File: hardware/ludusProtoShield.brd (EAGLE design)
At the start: 59.7 x 53.3 mm, 54 parts, among them U1 ARDUINO, U3 TB6612FNG

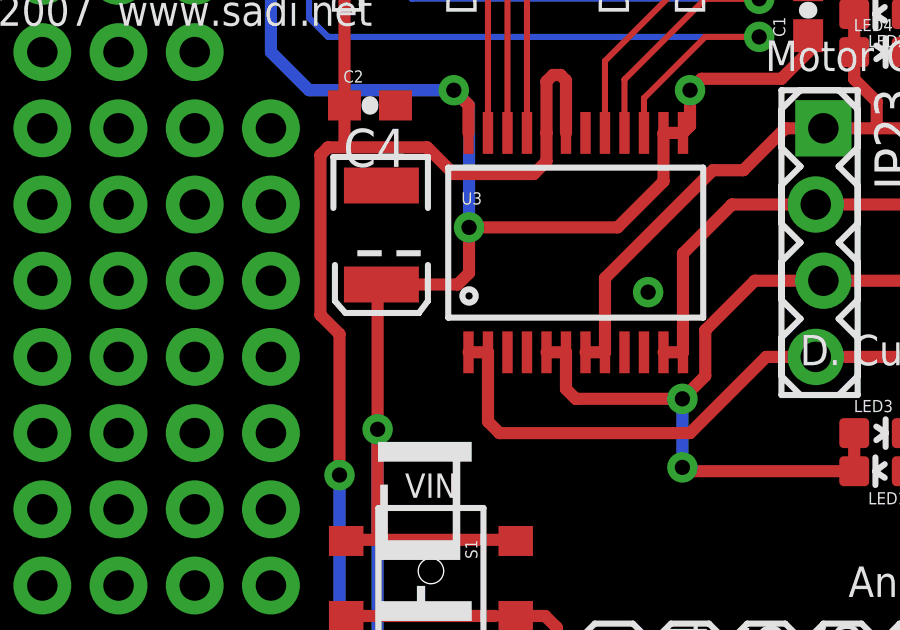
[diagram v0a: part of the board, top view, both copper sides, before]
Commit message: Fixed ERC & Board Consistency errors
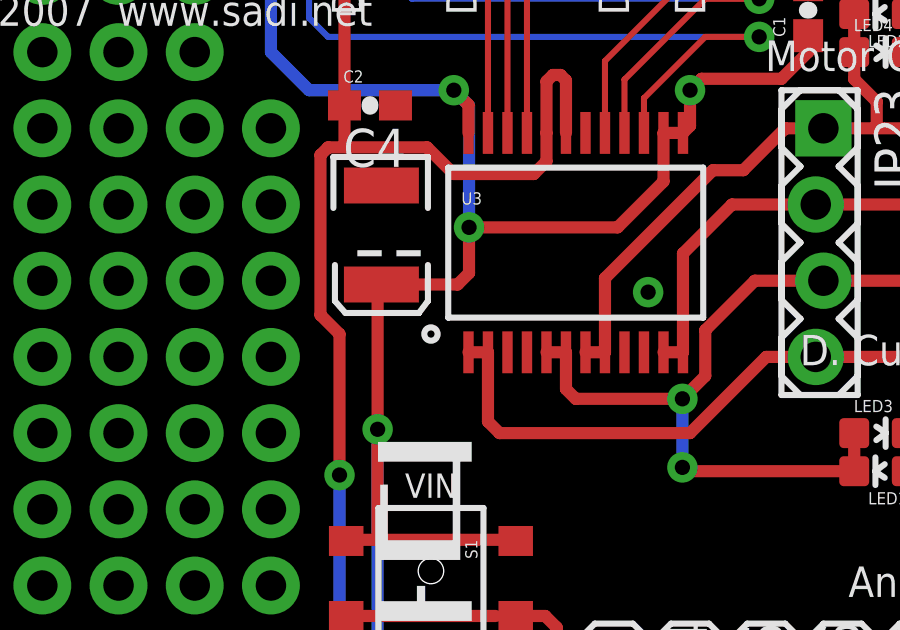
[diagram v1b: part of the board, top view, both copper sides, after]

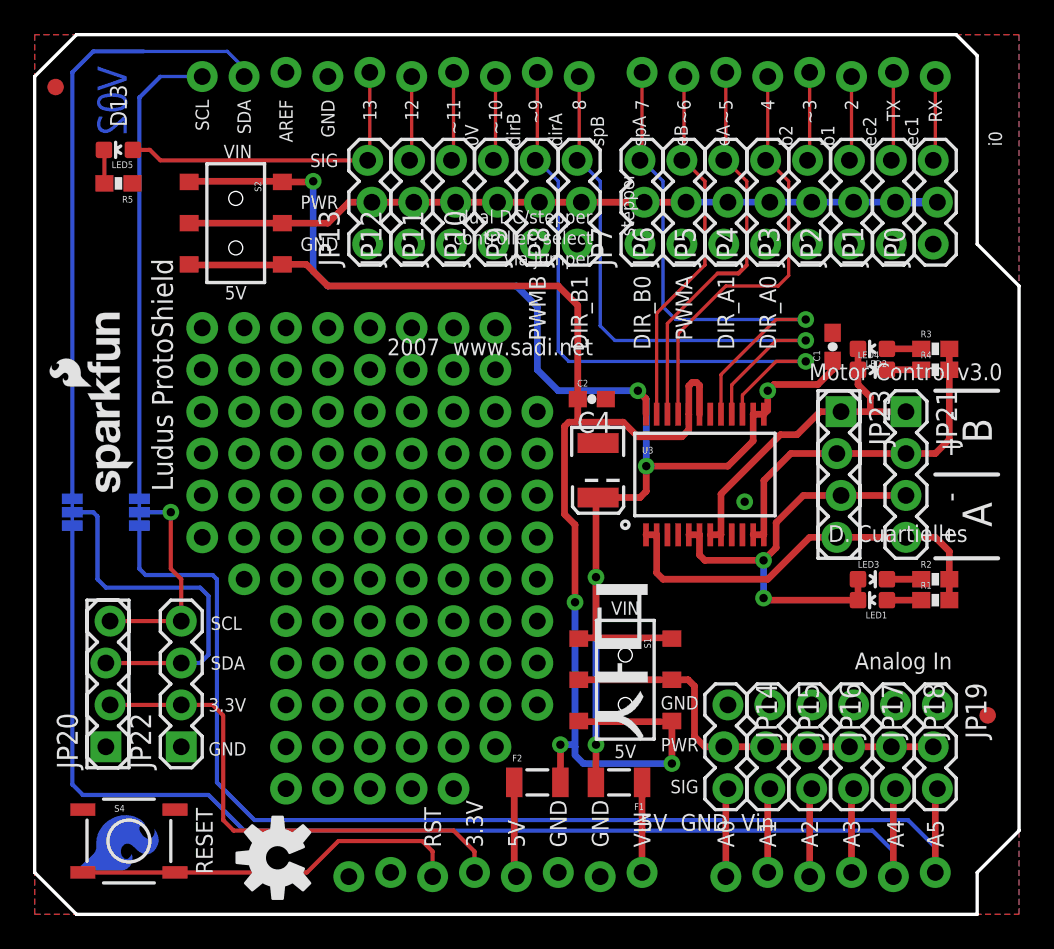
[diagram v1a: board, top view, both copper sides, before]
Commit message: Minor silk changes
Updated pin silks to 0.04 for all ones that don't interfere with other
masks.

Added to bSilk labels for the motor out
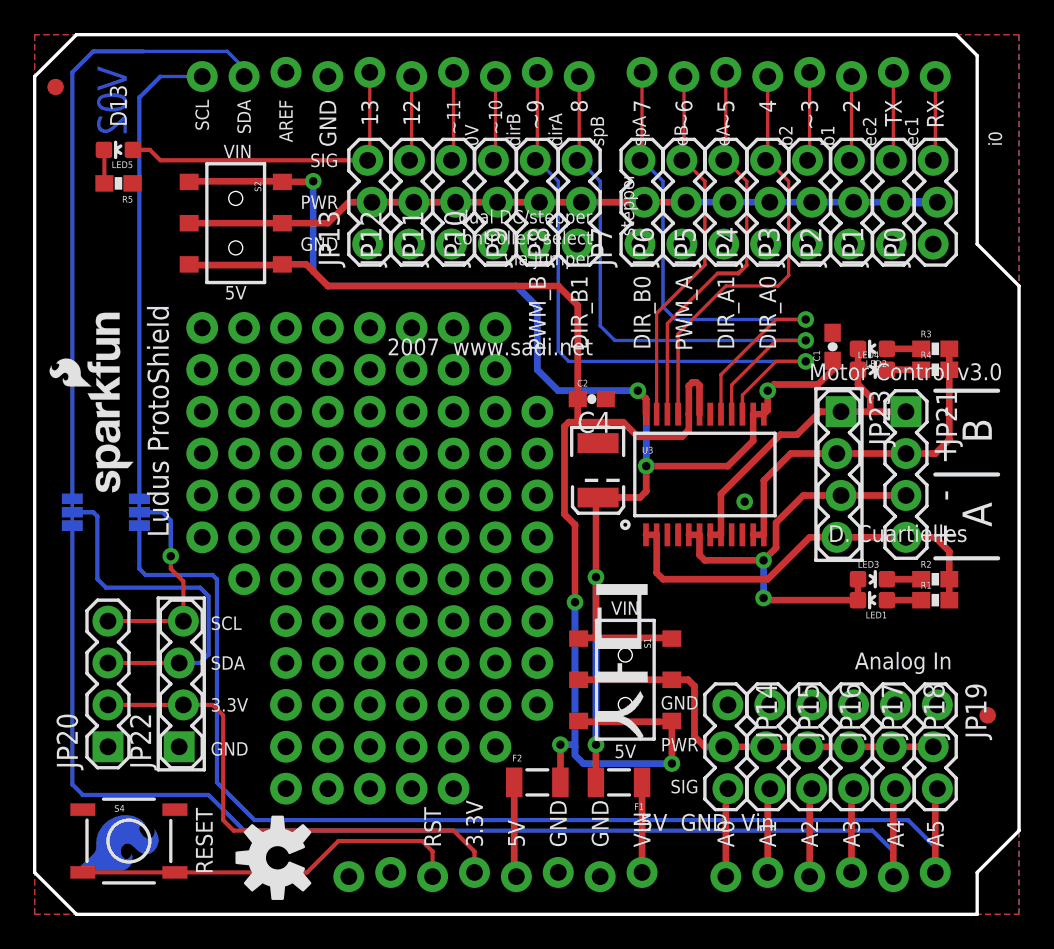
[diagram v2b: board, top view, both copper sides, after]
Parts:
- JP20: device SparkFun-Connectors:1X04_LOCK -> SparkFun-Connectors:1X04
- JP22: device SparkFun-Connectors:1X04 -> SparkFun-Connectors:1X04_LOCK
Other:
- board text added: "PWM_A"
- board text added: "PWM_B"
- board text removed: "PWMA"
- board text removed: "PWMB"

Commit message: Final changes to v1.0
Final design changes from engineering design review. Ready for reds.
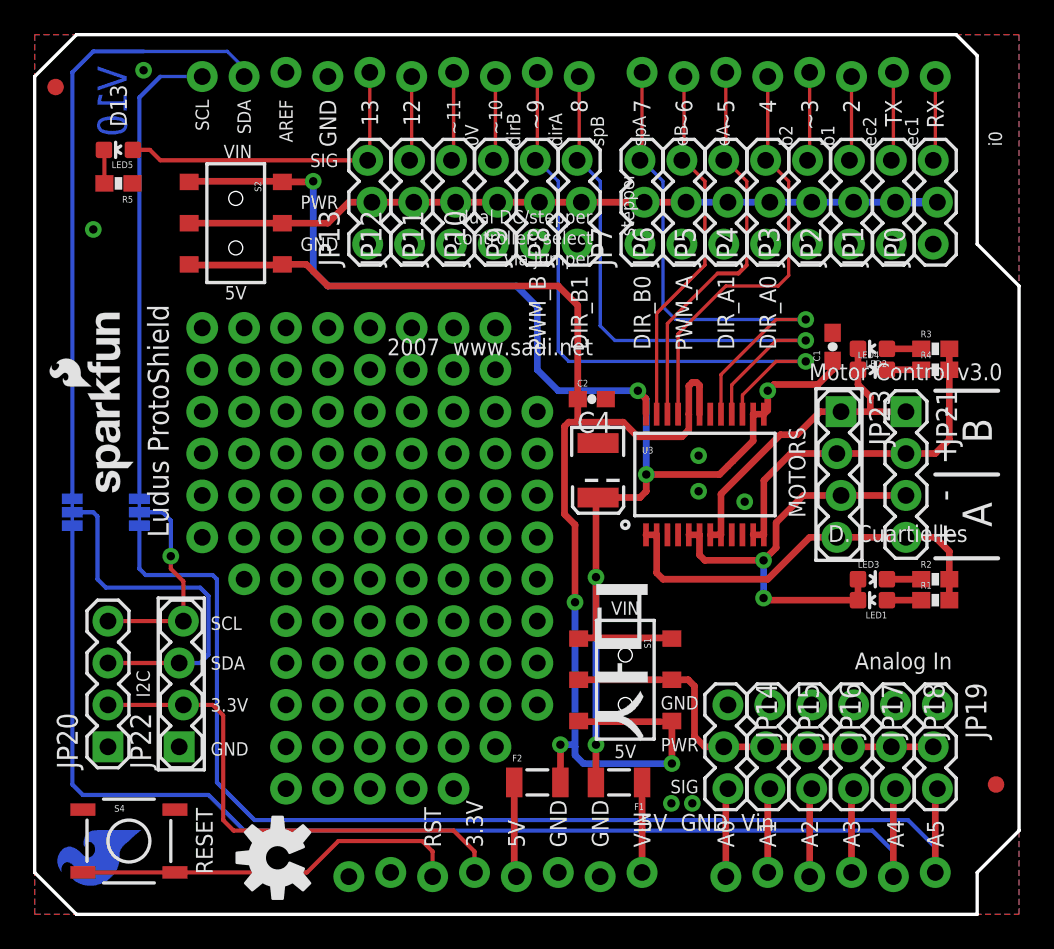
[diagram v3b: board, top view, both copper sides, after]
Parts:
- moved LOGO3 5.57 mm to (6.73, 5.46), turned to 270 degrees
- moved FID2 4.22 mm to (58.3, 7.87)
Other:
- board text added: "I2C"
- board text added: "MOTORS"
- board text added: "V10"
- board text removed: "V02"
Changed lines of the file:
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@@
 <text x="35.814" y="18.161" size="0.8128" layer="21" font="vector" ratio="15" align="bottom-center">VIN</text>
 <text x="35.814" y="10.287" size="0.8128" layer="21" font="vector" ratio="15" align="top-center">5V</text>
-<text x="5.588" y="51.435" size="1.778" layer="16" font="vector" ratio="15" rot="SMR270">V02</text>
+<text x="5.588" y="51.435" size="1.778" layer="16" font="vector" ratio="15" rot="SMR270">V10</text>
 <text x="37.211" y="-21.717" size="1.778" layer="51" font="vector" ratio="15">B. Huang</text>
 <text x="12.7" y="49.403" size="0.8128" layer="21" ratio="15" rot="R270" align="center-left">SDA</text>
@@
 <wire x1="56.261" y1="21.59" x2="54.61" y2="21.59" width="0.254" layer="22"/>
 <wire x1="56.261" y1="31.75" x2="54.61" y2="31.75" width="0.254" layer="22"/>
+<text x="46.736" y="26.797" size="1.016" layer="21" font="vector" ratio="15" rot="R90" align="bottom-center">MOTORS</text>
+<text x="6.985" y="13.97" size="0.8128" layer="21" font="vector" ratio="15" rot="R90" align="bottom-center">I2C</text>
+<text x="10.668" y="10.033" size="0.8128" layer="22" font="vector" ratio="15" rot="MR180" align="center-left">GND</text>
+<text x="10.668" y="12.7" size="0.8128" layer="22" font="vector" ratio="15" rot="MR180" align="center-left">3.3V</text>
+<text x="10.668" y="15.24" size="0.8128" layer="22" font="vector" ratio="15" rot="MR180" align="center-left">SDA</text>
+<text x="10.668" y="17.653" size="0.8128" layer="22" font="vector" ratio="15" rot="MR180" align="center-left">SCL</text>
+<text x="6.985" y="13.97" size="0.8128" layer="22" font="vector" ratio="15" rot="SMR270" align="bottom-center">I2C</text>
 </plain>
 <attributes>
@@
 </element>
 <element name="FID1" library="SparkFun-Aesthetics" package="FIDUCIAL-1X2" value="FIDUCIAL1X2" x="1.27" y="50.165"/>
-<element name="FID2" library="SparkFun-Aesthetics" package="FIDUCIAL-1X2" value="FIDUCIAL1X2" x="57.785" y="12.065"/>
+<element name="FID2" library="SparkFun-Aesthetics" package="FIDUCIAL-1X2" value="FIDUCIAL1X2" x="58.293" y="7.874"/>
 <element name="JP20" library="SparkFun-Connectors" package="1X04" value="" x="4.445" y="10.16" rot="R90"/>
 <element name="LOGO1" library="SparkFun-Aesthetics" package="OSHW-LOGO-M" value="OSHW-LOGOM" x="14.732" y="3.429" rot="R90"/>
@@
 <element name="SJ3" library="SparkFun-Passives" package="PAD-JUMPER-3-3OF3_NC_BY_TRACE_YES_SILK_FULL_BOX" value="" x="2.286" y="24.384" rot="MR270"/>
 <element name="SJ4" library="SparkFun-Passives" package="PAD-JUMPER-3-3OF3_NC_BY_TRACE_YES_SILK_FULL_BOX" value="" x="6.35" y="24.384" rot="MR270"/>
-<element name="LOGO3" library="SparkFun-Aesthetics" package="SFE_LOGO_FLAME_COPPER_.2" value="SFE_LOGO_FLAME.2COP" x="2.159" y="2.286" rot="SMR90"/>
 <element name="LOGO4" library="SparkFun-Aesthetics" package="SFE_LOGO_NAME_FLAME_.1" value="SFE_LOGO_NAME_FLAME.1_INCH" x="6.858" y="43.688" rot="MR270"/>
 <element name="JP23" library="SparkFun-Connectors" package="1X04_LOCK" value="" x="48.768" y="30.48" smashed="yes" rot="R270">
@@
 </element>
 <element name="U$1" library="SparkFun-Aesthetics" package="SFE_LUDUS-M" value="SFE_LUDUSSFE_LUDUS-M" x="41.275" y="26.67" rot="SMR270"/>
+<element name="LOGO3" library="SparkFun-Aesthetics" package="SFE_LOGO_FLAME_COPPER_.2" value="SFE_LOGO_FLAME.2COP" x="6.731" y="5.461" rot="MR270"/>
 </elements>
 <signals>
@@
 <contactref element="C2" pad="2"/>
 <via x="43.053" y="25.019" extent="1-16" drill="0.508"/>
+<via x="40.259" y="27.813" extent="1-16" drill="0.508"/>
+<via x="40.259" y="25.654" extent="1-16" drill="0.508"/>
+<via x="38.608" y="6.731" extent="1-16" drill="0.508"/>
+<via x="39.878" y="6.731" extent="1-16" drill="0.508"/>
+<via x="3.556" y="41.529" extent="1-16" drill="0.508"/>
+<via x="6.604" y="51.181" extent="1-16" drill="0.508"/>
 </signal>
 <signal name="D12">
@@
 <wire x1="30.48" y1="33.02" x2="31.75" y2="31.75" width="0.4064" layer="16"/>
 <wire x1="31.75" y1="31.75" x2="36.576" y2="31.75" width="0.4064" layer="16"/>
-<via x="37.084" y="27.178" extent="1-16" drill="0.508"/>
-<wire x1="37.084" y1="27.178" x2="37.084" y2="25.654" width="0.4064" layer="1"/>
+<via x="37.084" y="26.67" extent="1-16" drill="0.508"/>
+<wire x1="37.084" y1="26.67" x2="37.084" y2="25.654" width="0.4064" layer="1"/>
 <wire x1="37.084" y1="25.654" x2="36.704" y2="25.274" width="0.4064" layer="1"/>
 <wire x1="34.033" y1="25.144" x2="34.163" y2="25.274" width="0.4064" layer="1"/>
@@
 <wire x1="37.065" y1="30.326" x2="37.065" y2="31.261" width="0.4064" layer="1"/>
 <wire x1="37.065" y1="31.261" x2="36.576" y2="31.75" width="0.4064" layer="1"/>
-<wire x1="37.084" y1="27.178" x2="37.084" y2="31.242" width="0.4064" layer="16"/>
+<wire x1="37.084" y1="26.67" x2="37.084" y2="31.242" width="0.4064" layer="16"/>
 <wire x1="37.084" y1="31.242" x2="36.576" y2="31.75" width="0.4064" layer="16"/>
 <wire x1="43.565" y1="30.326" x2="43.565" y2="28.706" width="0.4064" layer="1"/>
-<wire x1="43.565" y1="28.706" x2="42.037" y2="27.178" width="0.4064" layer="1"/>
-<wire x1="42.037" y1="27.178" x2="37.084" y2="27.178" width="0.4064" layer="1"/>
+<wire x1="43.565" y1="28.706" x2="42.3545" y2="27.4955" width="0.4064" layer="1"/>
+<wire x1="42.3545" y1="27.4955" x2="42.037" y2="27.178" width="0.4064" layer="1"/>
 <wire x1="43.565" y1="30.326" x2="44.215" y2="30.326" width="0.4064" layer="1"/>
 <contactref element="S1" pad="1"/>
@@
 <wire x1="34.036" y1="16.764" x2="38.599" y2="16.764" width="0.4064" layer="1"/>
 <wire x1="38.599" y1="16.764" x2="38.639" y2="16.724" width="0.4064" layer="1"/>
+<wire x1="37.084" y1="26.67" x2="41.529" y2="26.67" width="0.4064" layer="1"/>
+<wire x1="41.529" y1="26.67" x2="42.037" y2="27.178" width="0.4064" layer="1"/>
 </signal>
 <signal name="FUSED_VCC">

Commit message: Updated libraries and fixed issues from QC for Reds
Updated all of the product libraries and cleaned up extra labels in
hidden layers per issues #10-14
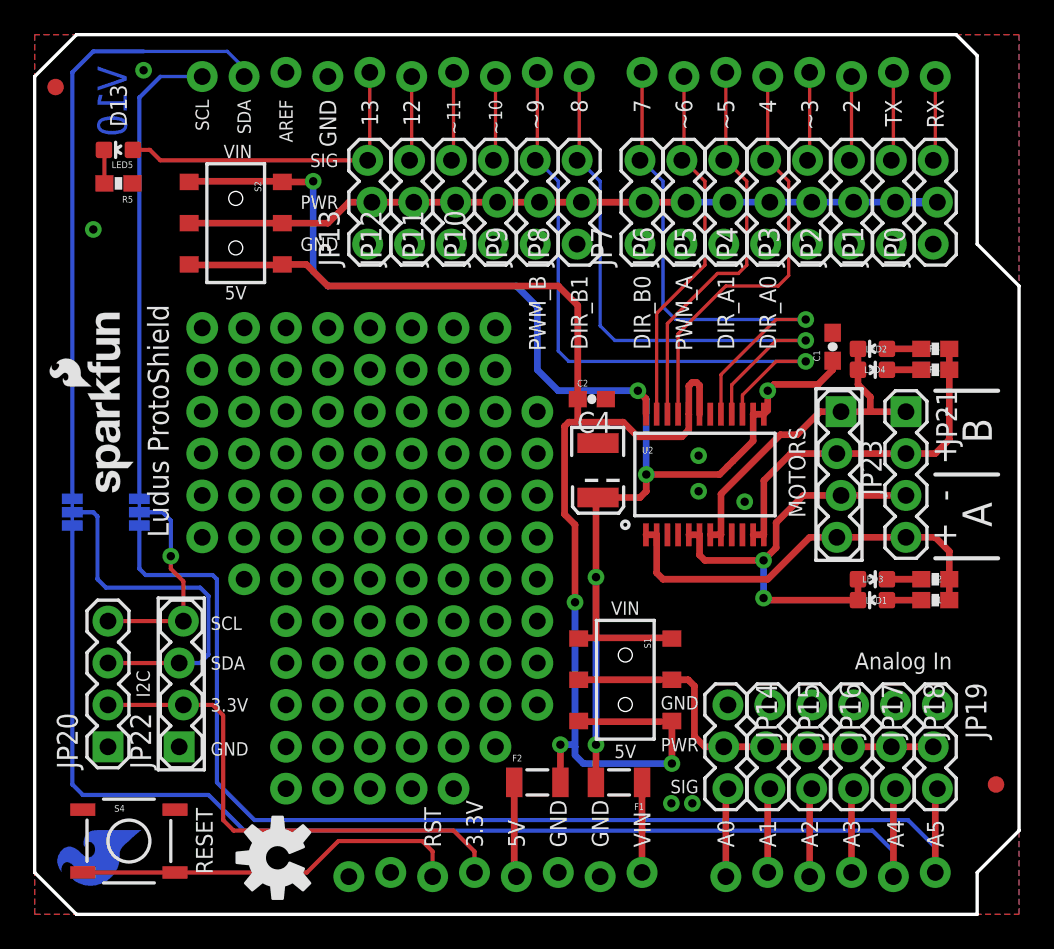
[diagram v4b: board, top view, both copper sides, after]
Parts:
- F1, F2: value PTCSMD -> (none)
- LED3, LED4: value Blue -> BLUE
- R1, R2, R3, R4: value 1k -> 1K
- renumbered U3 to U2
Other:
- board text removed: "0V"
- board text removed: "2007 www.sadi.net"
- board text removed: "5V GND Vin"
- board text removed: "D. Cuartielles"
- board text removed: "Motor Control v3.0"
- board text removed: "b1"
- board text removed: "b2"
- board text removed: "controller, select"
- board text removed: "dirA"
- board text removed: "dirB"
- board text removed: "dual DC/stepper"
- board text removed: "eA"
- board text removed: "eB"
- board text removed: "ec1"
- board text removed: "ec2"
- board text removed: "i0"
- board text removed: "spA"
- board text removed: "spB"
- board text removed: "stepper"
- board text removed: "via jumper"
